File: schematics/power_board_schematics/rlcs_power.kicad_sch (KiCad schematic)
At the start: 39 parts, among them J1 Conn_01x05_Male, J2 Conn_01x05_Male, J3 Screw_Terminal_01x02, J4 Battery Conn, J5 Battery Conn, J6 Screw_Terminal_01x02, J7 Screw_Terminal_01x02, J8 Keylock Switch Conn, Q1 Q_NPN_BEC, Q2 Q_NPN_BEC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

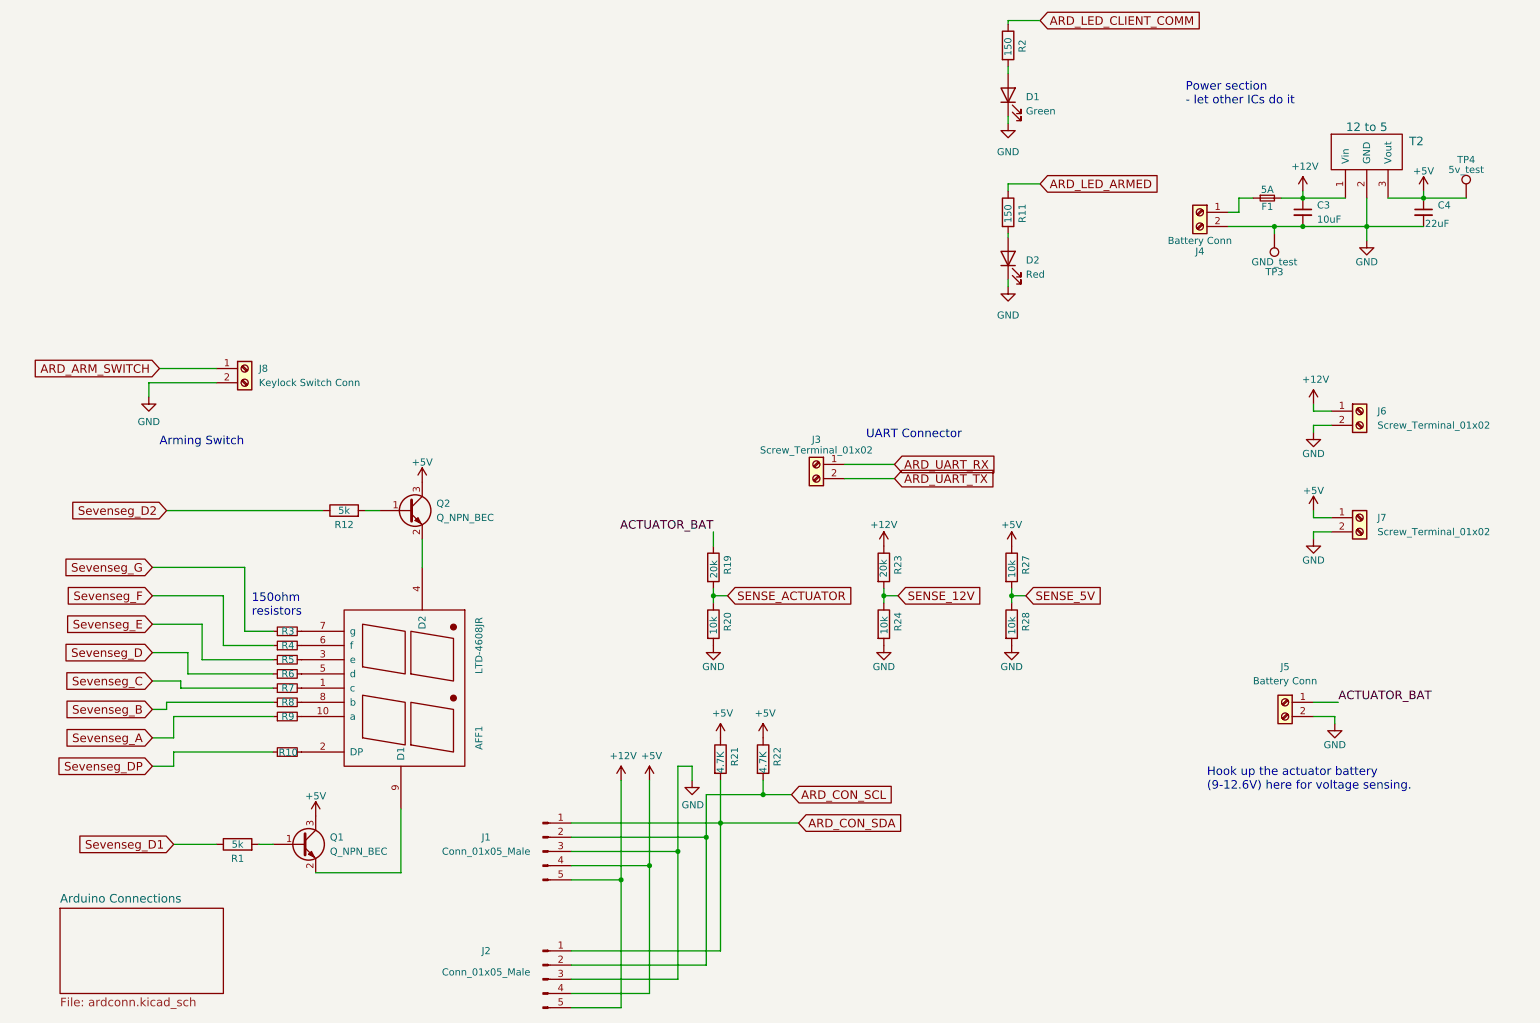
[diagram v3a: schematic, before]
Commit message: Reorganize Towerside Power Board schematics
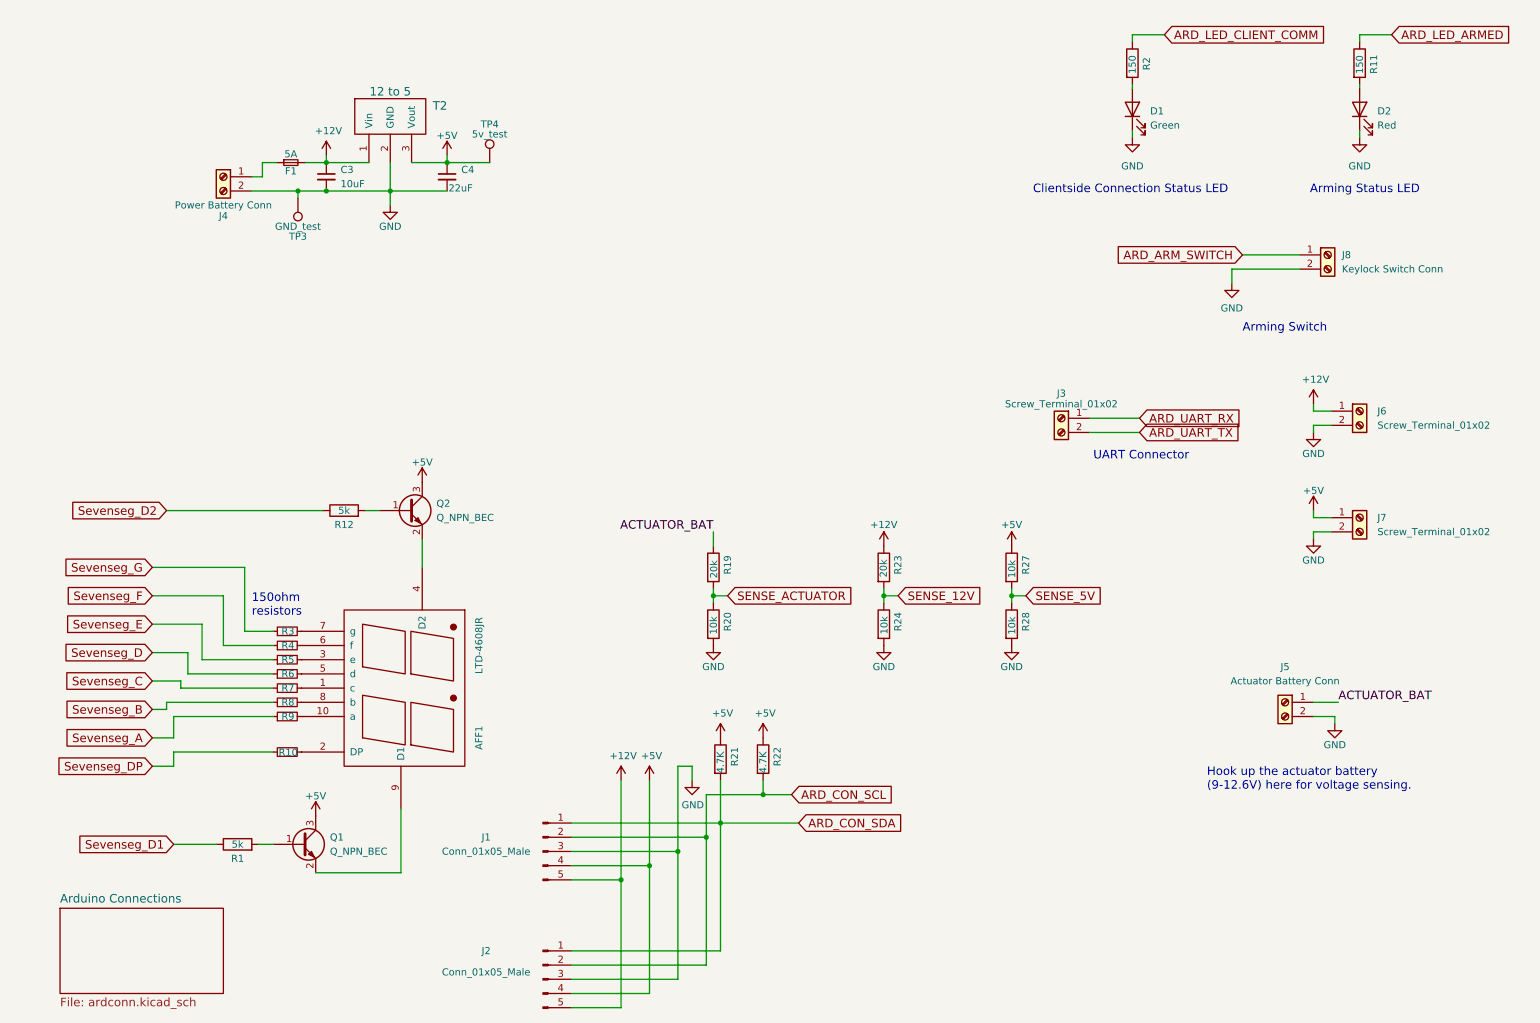
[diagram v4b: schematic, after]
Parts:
- J4: value Battery Conn -> Power Battery Conn
- J5: value Battery Conn -> Actuator Battery Conn
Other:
- note added: "Arming Status LED"
- note added: "Clientside Connection Status LED"
- note removed: "Power section - let other ICs do it"
- moved on the sheet: C3, C4, D1, D2, F1, J3, J4, J8, R11, R2, T2, TP3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

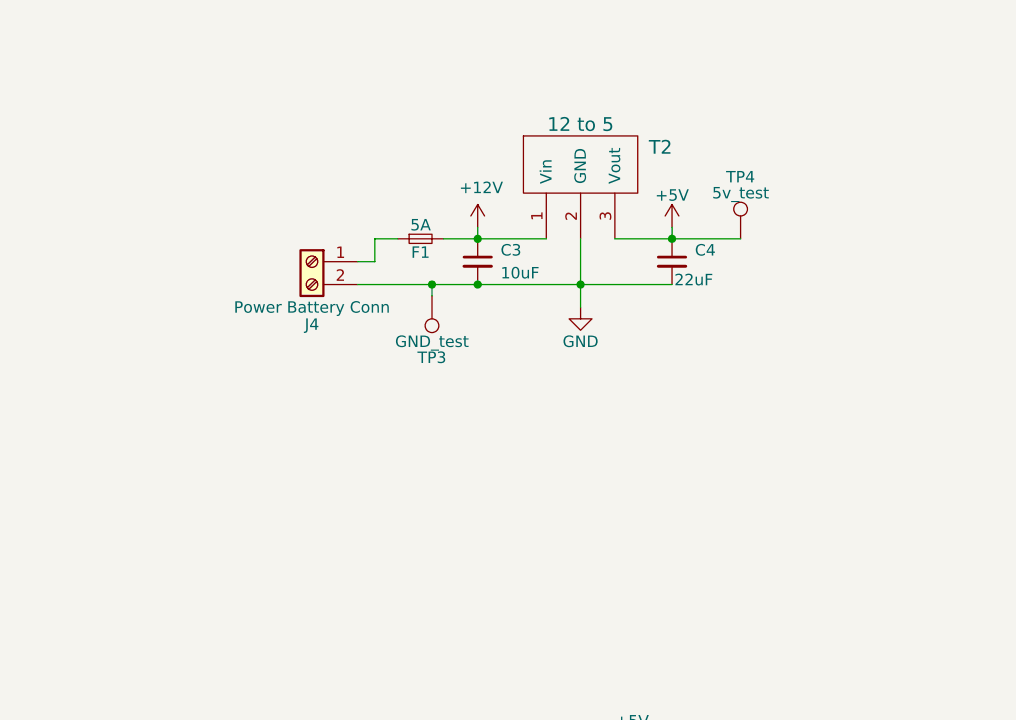
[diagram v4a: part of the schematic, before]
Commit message: Add power switch connector to Towerside Power Board
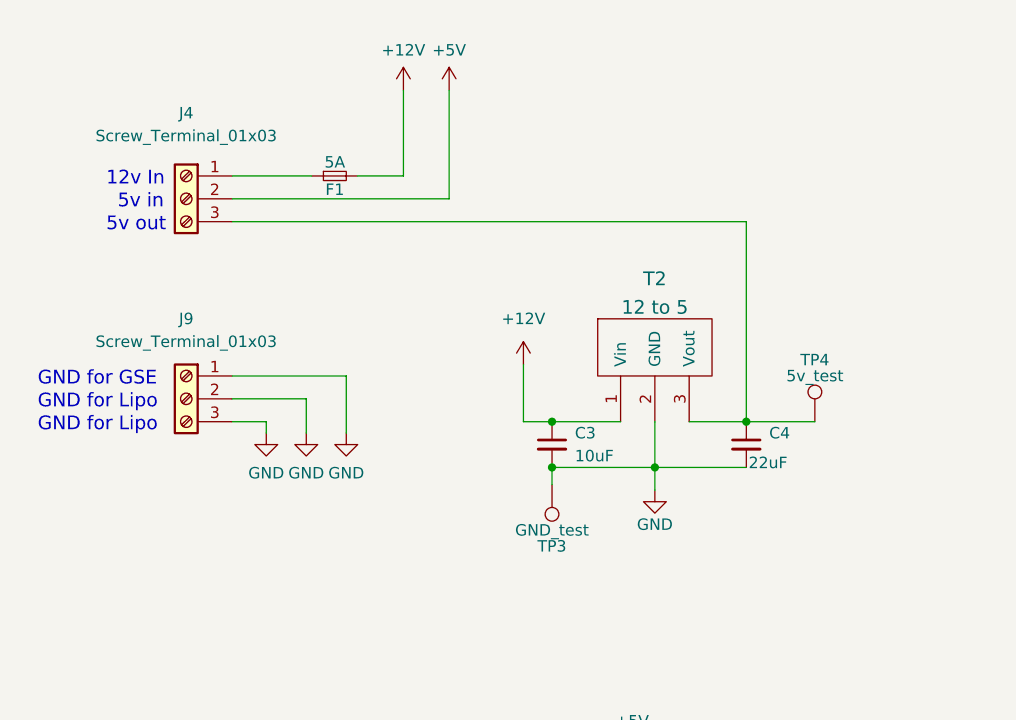
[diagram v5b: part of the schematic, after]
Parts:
- removed J4: Power Battery Conn, TerminalBlock_Phoenix:TerminalBlock_Phoenix_MKDS-1,5-2-5.08_1x02_P5.08mm_Horizontal, symbol Connector:Screw_Terminal_01x02
- added J4, J9: Screw_Terminal_01x03, TerminalBlock_Phoenix:TerminalBlock_Phoenix_MKDS-1,5-3-5.08_1x03_P5.08mm_Horizontal, symbol Connector:Screw_Terminal_01x03
- J8: footprint (none) -> TerminalBlock_Phoenix:TerminalBlock_Phoenix_PT-1,5-2-5.0-H_1x02_P5.00mm_Horizontal
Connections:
- net +5V: now also J4.2 (Pin_2); no longer C4.1, T2.3 (Vout), TP4.1
- net GND: now also J9.1 (Pin_1), J9.2 (Pin_2), J9.3 (Pin_3)
- net at F1.1: now also J4.1 (Pin_1)
- new net: C4.1, J4.3 (Pin_3), T2.3 (Vout), TP4.1
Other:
- note added: "12v In"
- note added: "5v in"
- note added: "5v out"
- note added: "GND for GSE"
- note added: "GND for Lipo"
- moved on the sheet: C3, C4, F1, T2, TP3, TP4
